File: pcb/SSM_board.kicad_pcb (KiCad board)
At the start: 4 copper layers, 100 x 100 mm, 115 parts, among them IC1 STPIC6C595TTR, IC2 STPIC6C595TTR, IC3 STPIC6C595TTR, IC4 STPIC6C595TTR, IC5 STPIC6C595TTR, J1 Conn_02x05_Top_Bottom, J2 Conn_02x05_Top_Bottom, U101 GAQY212GS, U102 GAQY212GS, U103 GAQY212GS, U104 GAQY212GS, U105 GAQY212GS, U106 GAQY212GS, U107 GAQY212GS, U108 GAQY212GS, U201 GAQY212GS, U202 GAQY212GS, U203 GAQY212GS, U204 GAQY212GS, U205 GAQY212GS, U206 GAQY212GS, U207 GAQY212GS, U208 GAQY212GS, U301 GAQY212GS, U302 GAQY212GS, U303 GAQY212GS, U304 GAQY212GS, U305 GAQY212GS, U306 GAQY212GS, U307 GAQY212GS, U308 GAQY212GS, U401 GAQY212GS, U402 GAQY212GS, U403 GAQY212GS, U404 GAQY212GS, U405 GAQY212GS, U406 GAQY212GS, U407 GAQY212GS, U408 GAQY212GS, U501 GAQY212GS, U502 GAQY212GS, U503 GAQY212GS, U504 GAQY212GS, U505 GAQY212GS, U506 GAQY212GS, U507 GAQY212GS, U508 GAQY212GS

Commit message: Functional block routing
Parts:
- removed J1, J2: Conn_02x05_Top_Bottom, Connector_IDC:IDC-Header_2x05_P2.54mm_Vertical
- added C6: 100n, Capacitor_SMD:C_0603_1608Metric_Pad1.08x0.95mm_HandSolder, F.Cu at (192.4, 129.0)
- added C7: 100n, Capacitor_SMD:C_0603_1608Metric_Pad1.08x0.95mm_HandSolder, F.Cu at (194.0, 137.6)
- added C8: 100n, Capacitor_SMD:C_0603_1608Metric_Pad1.08x0.95mm_HandSolder, F.Cu at (210.7, 129.0)
- added FB6: 100R @ 100MHz, Inductor_SMD:L_0603_1608Metric, F.Cu at (192.5, 125.6)
- added FB7: 100R @ 100MHz, Inductor_SMD:L_0603_1608Metric, F.Cu at (197.8, 141.5)
- added FB8: 100R @ 100MHz, Inductor_SMD:L_0603_1608Metric, F.Cu at (210.7, 125.8)
- added IC6: STPIC6C595TTR, SamacSys_Parts:SOP65P640X120-16N, F.Cu at (188.7, 131.1)
- added IC7: STPIC6C595TTR, SamacSys_Parts:SOP65P640X120-16N, F.Cu at (198.5, 130.9)
- added IC8: STPIC6C595TTR, SamacSys_Parts:SOP65P640X120-16N, F.Cu at (207.0, 131.1)
- added J701: DA15_Pins_MountingHoles, Connector_Dsub:DSUB-15_Pins_Horizontal_P2.77x2.84mm_EdgePinOffset4.94mm_Housed_MountingHolesOffset4.94mm, F.Cu at (77.8, 70.1)
- added J702: DA15_Pins_MountingHoles, Connector_Dsub:DSUB-15_Pins_Horizontal_P2.77x2.84mm_EdgePinOffset4.94mm_Housed_MountingHolesOffset4.94mm, F.Cu at (77.8, 110.5)
- added R6: 10k, Resistor_SMD:R_0603_1608Metric_Pad0.98x0.95mm_HandSolder, F.Cu at (191.0, 125.4)
- added R601: 50k, Resistor_SMD:R_0603_1608Metric_Pad0.98x0.95mm_HandSolder, F.Cu at (189.9, 96.1)
- added R602: 50k, Resistor_SMD:R_0603_1608Metric_Pad0.98x0.95mm_HandSolder, F.Cu at (189.9, 91.4)
- added R603: 50k, Resistor_SMD:R_0603_1608Metric_Pad0.98x0.95mm_HandSolder, F.Cu at (189.9, 86.8)
- added R604: 50k, Resistor_SMD:R_0603_1608Metric_Pad0.98x0.95mm_HandSolder, F.Cu at (189.9, 82.1)
- added R605: 50k, Resistor_SMD:R_0603_1608Metric_Pad0.98x0.95mm_HandSolder, F.Cu at (189.9, 63.5)
- added R606: 50k, Resistor_SMD:R_0603_1608Metric_Pad0.98x0.95mm_HandSolder, F.Cu at (189.9, 68.2)
- added R607: 50k, Resistor_SMD:R_0603_1608Metric_Pad0.98x0.95mm_HandSolder, F.Cu at (189.9, 72.8)
- added R608: 50k, Resistor_SMD:R_0603_1608Metric_Pad0.98x0.95mm_HandSolder, F.Cu at (189.9, 77.5)
- added R609: 50k, Resistor_SMD:R_0603_1608Metric_Pad0.98x0.95mm_HandSolder, F.Cu at (189.9, 114.7)
- added R610: 50k, Resistor_SMD:R_0603_1608Metric_Pad0.98x0.95mm_HandSolder, F.Cu at (189.9, 110.0)
- added R611: 50k, Resistor_SMD:R_0603_1608Metric_Pad0.98x0.95mm_HandSolder, F.Cu at (189.9, 105.4)
- added R612: 50k, Resistor_SMD:R_0603_1608Metric_Pad0.98x0.95mm_HandSolder, F.Cu at (189.9, 100.7)
- added R7: 10k, Resistor_SMD:R_0603_1608Metric_Pad0.98x0.95mm_HandSolder, F.Cu at (197.0, 137.8)
- added R701: 50k, Resistor_SMD:R_0603_1608Metric_Pad0.98x0.95mm_HandSolder, F.Cu at (205.6, 63.8)
- added R702: 50k, Resistor_SMD:R_0603_1608Metric_Pad0.98x0.95mm_HandSolder, F.Cu at (205.6, 68.5)
- added R703: 50k, Resistor_SMD:R_0603_1608Metric_Pad0.98x0.95mm_HandSolder, F.Cu at (205.6, 73.1)
- added R704: 50k, Resistor_SMD:R_0603_1608Metric_Pad0.98x0.95mm_HandSolder, F.Cu at (205.6, 77.8)
- added R705: 50k, Resistor_SMD:R_0603_1608Metric_Pad0.98x0.95mm_HandSolder, F.Cu at (205.6, 115.0)
- added R706: 50k, Resistor_SMD:R_0603_1608Metric_Pad0.98x0.95mm_HandSolder, F.Cu at (205.6, 110.3)
- added R707: 50k, Resistor_SMD:R_0603_1608Metric_Pad0.98x0.95mm_HandSolder, F.Cu at (205.6, 105.7)
- added R708: 50k, Resistor_SMD:R_0603_1608Metric_Pad0.98x0.95mm_HandSolder, F.Cu at (205.6, 101.0)
- added R709: 50k, Resistor_SMD:R_0603_1608Metric_Pad0.98x0.95mm_HandSolder, F.Cu at (205.6, 82.4)
- added R710: 50k, Resistor_SMD:R_0603_1608Metric_Pad0.98x0.95mm_HandSolder, F.Cu at (205.6, 87.1)
- added R711: 50k, Resistor_SMD:R_0603_1608Metric_Pad0.98x0.95mm_HandSolder, F.Cu at (205.6, 91.7)
- added R712: 50k, Resistor_SMD:R_0603_1608Metric_Pad0.98x0.95mm_HandSolder, F.Cu at (205.6, 96.4)
- added R8: 10k, Resistor_SMD:R_0603_1608Metric_Pad0.98x0.95mm_HandSolder, F.Cu at (209.1, 125.5)
- added RN11: 470R, Resistor_SMD:R_Array_Convex_4x0603, F.Cu at (188.3, 125.0)
- added RN12: 470R, Resistor_SMD:R_Array_Convex_4x0603, F.Cu at (185.3, 121.9)
- added RN13: 470R, Resistor_SMD:R_Array_Convex_4x0603, F.Cu at (195.1, 125.1)
- added RN14: 470R, Resistor_SMD:R_Array_Convex_4x0603, F.Cu at (198.9, 125.1)
- added RN15: 470R, Resistor_SMD:R_Array_Convex_4x0603, F.Cu at (206.5, 125.1)
- added RN16: 470R, Resistor_SMD:R_Array_Convex_4x0603, F.Cu at (202.8, 125.1)
- added U601: GAQY212GS, Package_SO:SOP-4_3.8x4.1mm_P2.54mm, F.Cu at (194.4, 96.1)
- added U602: GAQY212GS, Package_SO:SOP-4_3.8x4.1mm_P2.54mm, F.Cu at (194.4, 91.4)
- added U603: GAQY212GS, Package_SO:SOP-4_3.8x4.1mm_P2.54mm, F.Cu at (194.4, 86.8)
- added U604: GAQY212GS, Package_SO:SOP-4_3.8x4.1mm_P2.54mm, F.Cu at (194.4, 82.1)
- added U605: GAQY212GS, Package_SO:SOP-4_3.8x4.1mm_P2.54mm, F.Cu at (194.4, 63.5)
- added U606: GAQY212GS, Package_SO:SOP-4_3.8x4.1mm_P2.54mm, F.Cu at (194.4, 68.2)
- added U607: GAQY212GS, Package_SO:SOP-4_3.8x4.1mm_P2.54mm, F.Cu at (194.4, 72.8)
- added U608: GAQY212GS, Package_SO:SOP-4_3.8x4.1mm_P2.54mm, F.Cu at (194.4, 77.5)
- added U609: GAQY212GS, Package_SO:SOP-4_3.8x4.1mm_P2.54mm, F.Cu at (194.4, 114.7)
- added U610: GAQY212GS, Package_SO:SOP-4_3.8x4.1mm_P2.54mm, F.Cu at (194.4, 110.0)
- added U611: GAQY212GS, Package_SO:SOP-4_3.8x4.1mm_P2.54mm, F.Cu at (194.4, 105.4)
- added U612: GAQY212GS, Package_SO:SOP-4_3.8x4.1mm_P2.54mm, F.Cu at (194.4, 100.7)
- added U701: GAQY212GS, Package_SO:SOP-4_3.8x4.1mm_P2.54mm, F.Cu at (210.1, 63.8)
- added U702: GAQY212GS, Package_SO:SOP-4_3.8x4.1mm_P2.54mm, F.Cu at (210.1, 68.5)
- added U703: GAQY212GS, Package_SO:SOP-4_3.8x4.1mm_P2.54mm, F.Cu at (210.1, 73.1)
- added U704: GAQY212GS, Package_SO:SOP-4_3.8x4.1mm_P2.54mm, F.Cu at (210.1, 77.8)
- added U705: GAQY212GS, Package_SO:SOP-4_3.8x4.1mm_P2.54mm, F.Cu at (210.1, 115.0)
- added U706: GAQY212GS, Package_SO:SOP-4_3.8x4.1mm_P2.54mm, F.Cu at (210.1, 110.3)
- added U707: GAQY212GS, Package_SO:SOP-4_3.8x4.1mm_P2.54mm, F.Cu at (210.1, 105.7)
- added U708: GAQY212GS, Package_SO:SOP-4_3.8x4.1mm_P2.54mm, F.Cu at (210.1, 101.0)
- added U709: GAQY212GS, Package_SO:SOP-4_3.8x4.1mm_P2.54mm, F.Cu at (210.1, 82.4)
- added U710: GAQY212GS, Package_SO:SOP-4_3.8x4.1mm_P2.54mm, F.Cu at (210.1, 87.1)
- added U711: GAQY212GS, Package_SO:SOP-4_3.8x4.1mm_P2.54mm, F.Cu at (210.1, 91.7)
- added U712: GAQY212GS, Package_SO:SOP-4_3.8x4.1mm_P2.54mm, F.Cu at (210.1, 96.4)
- moved R505 140.9 mm to (118.0, 67.6)
- moved FB5 137.8 mm to (156.3, 64.6), turned to 180 degrees
- moved R506 136.8 mm to (122.6, 67.6)
- moved R5 134.9 mm to (156.1, 66.1)
- moved R405 134.6 mm to (118.0, 83.4)
- moved R507 132.8 mm to (127.3, 67.6)
- moved C5 131.2 mm to (159.7, 65.0), turned to 180 degrees
- moved R406 130.1 mm to (122.6, 83.4)
- moved R305 130.1 mm to (118.0, 99.1)
- moved R508 128.9 mm to (131.9, 67.6)
- moved IC5 127.0 mm to (161.7, 68.7)
- moved R407 125.8 mm to (127.3, 83.4)
- moved R306 125.3 mm to (122.6, 99.1)
- moved R504 122.1 mm to (136.6, 67.6)
- moved R408 121.5 mm to (131.9, 83.4)
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- renumbered R102 to R101, R103 to R102, R104 to R103, R105 to R104, R106 to R105, R107 to R106, R108 to R107, R109 to R108
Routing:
- net +5V: track 134.1 -> 385.1 mm
- net /Frontend/701: track 0.00 -> 62.7 mm
- net /Frontend/605: track 0.00 -> 58.9 mm
- net /Frontend/702: track 0.00 -> 57.7 mm
- net /Frontend/606: track 0.00 -> 54.1 mm
- net /Frontend/703: track 0.00 -> 52.7 mm
- net /Frontend/607: track 0.00 -> 49.4 mm
- net /Frontend/704: track 0.00 -> 47.7 mm
- net /Frontend/608: track 0.00 -> 44.6 mm
- net /Frontend/604: track 0.00 -> 43.0 mm
- net /Frontend/709: track 0.00 -> 42.5 mm
- net /Frontend/505: track 0.00 -> 40.9 mm
- net /Frontend/305: track 0.00 -> 40.8 mm
- net /Frontend/405: track 0.00 -> 40.8 mm
- net /Frontend/603: track 0.00 -> 38.3 mm
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
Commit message: More routing
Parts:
- moved R7 106.7 mm to (90.3, 140.5), turned to 90 degrees
- moved FB7 105.3 mm to (93.4, 127.1), turned to 90 degrees
- moved IC7 102.7 mm to (96.1, 138.9)
- moved IC6 102.7 mm to (86.3, 138.2)
- moved R701 102.7 mm to (103.2, 71.0)
- moved R702 102.7 mm to (103.2, 75.7)
- moved R703 102.7 mm to (103.2, 80.3)
- moved R704 102.7 mm to (103.2, 85.0)
- moved R705 102.7 mm to (103.2, 122.2)
- moved R706 102.7 mm to (103.2, 117.5)
- moved R707 102.7 mm to (103.2, 112.9)
- moved R708 102.7 mm to (103.2, 108.2)
- moved R709 102.7 mm to (103.2, 89.6)
- moved R710 102.7 mm to (103.2, 94.3)
- moved R711 102.7 mm to (103.2, 98.9)
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- renumbered J701 to J1, J702 to J2
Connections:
- J1 pad 1: Net-(J701-Pad1) -> Net-(J1-Pad1)
- J1 pad 10: Net-(J701-P10) -> Net-(J1-P10)
- J1 pad 11: Net-(J701-P111) -> Net-(J1-P111)
- J1 pad 12: Net-(J701-P12) -> Net-(J1-P12)
- J1 pad 13: Net-(J701-P13) -> Net-(J1-P13)
- J1 pad 14: Net-(J701-P14) -> Earth_Protective
- J1 pad 2: Net-(J701-Pad2) -> Net-(J1-Pad2)
- J1 pad 3: Net-(J701-Pad3) -> Net-(J1-Pad3)
- J1 pad 4: Net-(J701-Pad4) -> Net-(J1-Pad4)
- J1 pad 5: Net-(J701-Pad5) -> Net-(J1-Pad5)
- J1 pad 6: Net-(J701-Pad6) -> Net-(J1-Pad6)
- J1 pad 7: Net-(J701-Pad7) -> Net-(J1-Pad7)
- J1 pad 8: Net-(J701-Pad8) -> Net-(J1-Pad8)
- J1 pad 9: Net-(J701-P9) -> Net-(J1-P9)
- J2 pad 1: Net-(J702-Pad1) -> Net-(J2-Pad1)
- J2 pad 10: Net-(J702-P10) -> Net-(J2-P10)
- J2 pad 11: Net-(J702-P111) -> Net-(J2-P111)
- J2 pad 12: Net-(J702-P12) -> Net-(J2-P12)
- J2 pad 13: Net-(J702-P13) -> Net-(J2-P13)
- J2 pad 14: unconnected-(J702-P14-Pad14) -> Net-(J2-P14)
- J2 pad 15: unconnected-(J702-P15-Pad15) -> Earth_Protective
- J2 pad 2: Net-(J702-Pad2) -> Net-(J2-Pad2)
- J2 pad 3: Net-(J702-Pad3) -> Net-(J2-Pad3)
- J2 pad 4: Net-(J702-Pad4) -> Net-(J2-Pad4)
- J2 pad 5: Net-(J702-Pad5) -> Net-(J2-Pad5)
- J2 pad 6: Net-(J702-Pad6) -> Net-(J2-Pad6)
- J2 pad 7: Net-(J702-Pad7) -> Net-(J2-Pad7)
- J2 pad 8: Net-(J702-Pad8) -> Net-(J2-Pad8)
- J2 pad 9: Net-(J702-P9) -> Net-(J2-P9)
- U101 pad 3: Net-(J702-Pad6) -> Net-(J1-Pad6)
- U101 pad 4: Net-(J702-Pad1) -> Net-(J1-Pad1)
- U102 pad 3: Net-(J702-Pad7) -> Net-(J1-Pad7)
- U102 pad 4: Net-(J702-Pad1) -> Net-(J1-Pad1)
- U103 pad 3: Net-(J702-Pad8) -> Net-(J1-Pad8)
- U103 pad 4: Net-(J702-Pad1) -> Net-(J1-Pad1)
- U104 pad 3: Net-(J702-P9) -> Net-(J1-P9)
- U104 pad 4: Net-(J702-Pad1) -> Net-(J1-Pad1)
- U105 pad 3: Net-(J702-P10) -> Net-(J1-P10)
- U105 pad 4: Net-(J702-Pad1) -> Net-(J1-Pad1)
- U106 pad 3: Net-(J702-P111) -> Net-(J1-P111)
- U106 pad 4: Net-(J702-Pad1) -> Net-(J1-Pad1)
- U107 pad 3: Net-(J702-P12) -> Net-(J1-P12)
- U107 pad 4: Net-(J702-Pad1) -> Net-(J1-Pad1)
- U108 pad 3: Net-(J702-P13) -> Net-(J1-P13)
- U108 pad 4: Net-(J702-Pad1) -> Net-(J1-Pad1)
- U201 pad 3: Net-(J702-Pad6) -> Net-(J1-Pad6)
- U201 pad 4: Net-(J702-Pad2) -> Net-(J1-Pad2)
- U202 pad 3: Net-(J702-Pad7) -> Net-(J1-Pad7)
- U202 pad 4: Net-(J702-Pad2) -> Net-(J1-Pad2)
- U203 pad 3: Net-(J702-Pad8) -> Net-(J1-Pad8)
- U203 pad 4: Net-(J702-Pad2) -> Net-(J1-Pad2)
- U204 pad 3: Net-(J702-P9) -> Net-(J1-P9)
- U204 pad 4: Net-(J702-Pad2) -> Net-(J1-Pad2)
- U205 pad 3: Net-(J702-P10) -> Net-(J1-P10)
- U205 pad 4: Net-(J702-Pad2) -> Net-(J1-Pad2)
- U206 pad 3: Net-(J702-P111) -> Net-(J1-P111)
- U206 pad 4: Net-(J702-Pad2) -> Net-(J1-Pad2)
- U207 pad 3: Net-(J702-P12) -> Net-(J1-P12)
- U207 pad 4: Net-(J702-Pad2) -> Net-(J1-Pad2)
- U208 pad 3: Net-(J702-P13) -> Net-(J1-P13)
- U208 pad 4: Net-(J702-Pad2) -> Net-(J1-Pad2)
- U301 pad 3: Net-(J702-Pad6) -> Net-(J1-Pad6)
- U301 pad 4: Net-(J702-Pad3) -> Net-(J1-Pad3)
- U302 pad 3: Net-(J702-Pad7) -> Net-(J1-Pad7)
- U302 pad 4: Net-(J702-Pad3) -> Net-(J1-Pad3)
- U303 pad 3: Net-(J702-Pad8) -> Net-(J1-Pad8)
- U303 pad 4: Net-(J702-Pad3) -> Net-(J1-Pad3)
- U304 pad 3: Net-(J702-P9) -> Net-(J1-P9)
- U304 pad 4: Net-(J702-Pad3) -> Net-(J1-Pad3)
- U305 pad 3: Net-(J702-P10) -> Net-(J1-P10)
- U305 pad 4: Net-(J702-Pad3) -> Net-(J1-Pad3)
- U306 pad 3: Net-(J702-P111) -> Net-(J1-P111)
- U306 pad 4: Net-(J702-Pad3) -> Net-(J1-Pad3)
- U307 pad 3: Net-(J702-P12) -> Net-(J1-P12)
- U307 pad 4: Net-(J702-Pad3) -> Net-(J1-Pad3)
- U308 pad 3: Net-(J702-P13) -> Net-(J1-P13)
- U308 pad 4: Net-(J702-Pad3) -> Net-(J1-Pad3)
- U401 pad 3: Net-(J702-Pad6) -> Net-(J1-Pad6)
- U401 pad 4: Net-(J702-Pad4) -> Net-(J1-Pad4)
- U402 pad 3: Net-(J702-Pad7) -> Net-(J1-Pad7)
- U402 pad 4: Net-(J702-Pad4) -> Net-(J1-Pad4)
- U403 pad 3: Net-(J702-Pad8) -> Net-(J1-Pad8)
- U403 pad 4: Net-(J702-Pad4) -> Net-(J1-Pad4)
- U404 pad 3: Net-(J702-P9) -> Net-(J1-P9)
- U404 pad 4: Net-(J702-Pad4) -> Net-(J1-Pad4)
- U405 pad 3: Net-(J702-P10) -> Net-(J1-P10)
- U405 pad 4: Net-(J702-Pad4) -> Net-(J1-Pad4)
- U406 pad 3: Net-(J702-P111) -> Net-(J1-P111)
- U406 pad 4: Net-(J702-Pad4) -> Net-(J1-Pad4)
- U407 pad 3: Net-(J702-P12) -> Net-(J1-P12)
- U407 pad 4: Net-(J702-Pad4) -> Net-(J1-Pad4)
- U408 pad 3: Net-(J702-P13) -> Net-(J1-P13)
- U408 pad 4: Net-(J702-Pad4) -> Net-(J1-Pad4)
- U501 pad 3: Net-(J702-Pad6) -> Net-(J1-Pad6)
- U501 pad 4: Net-(J702-Pad5) -> Net-(J1-Pad5)
- U502 pad 3: Net-(J702-Pad7) -> Net-(J1-Pad7)
- U502 pad 4: Net-(J702-Pad5) -> Net-(J1-Pad5)
- U503 pad 3: Net-(J702-Pad8) -> Net-(J1-Pad8)
- U503 pad 4: Net-(J702-Pad5) -> Net-(J1-Pad5)
- U504 pad 3: Net-(J702-P9) -> Net-(J1-P9)
- U504 pad 4: Net-(J702-Pad5) -> Net-(J1-Pad5)
- U505 pad 3: Net-(J702-P10) -> Net-(J1-P10)
- U505 pad 4: Net-(J702-Pad5) -> Net-(J1-Pad5)
- U506 pad 3: Net-(J702-P111) -> Net-(J1-P111)
- U506 pad 4: Net-(J702-Pad5) -> Net-(J1-Pad5)
- U507 pad 3: Net-(J702-P12) -> Net-(J1-P12)
- U507 pad 4: Net-(J702-Pad5) -> Net-(J1-Pad5)
- U508 pad 3: Net-(J702-P13) -> Net-(J1-P13)
- U508 pad 4: Net-(J702-Pad5) -> Net-(J1-Pad5)
- U601 pad 3: Net-(J701-Pad3) -> Net-(J2-Pad3)
- U601 pad 4: Net-(J701-Pad1) -> Net-(J2-Pad1)
- U602 pad 3: Net-(J701-Pad4) -> Net-(J2-Pad4)
- U602 pad 4: Net-(J701-Pad1) -> Net-(J2-Pad1)
- U603 pad 3: Net-(J701-Pad5) -> Net-(J2-Pad5)
- U603 pad 4: Net-(J701-Pad1) -> Net-(J2-Pad1)
- U604 pad 3: Net-(J701-Pad6) -> Net-(J2-Pad6)
- U604 pad 4: Net-(J701-Pad1) -> Net-(J2-Pad1)
- U605 pad 3: Net-(J701-Pad7) -> Net-(J2-Pad7)
- U605 pad 4: Net-(J701-Pad1) -> Net-(J2-Pad1)
- U606 pad 3: Net-(J701-Pad8) -> Net-(J2-Pad8)
- U606 pad 4: Net-(J701-Pad1) -> Net-(J2-Pad1)
- U607 pad 3: Net-(J701-P9) -> Net-(J2-P9)
- U607 pad 4: Net-(J701-Pad1) -> Net-(J2-Pad1)
- U608 pad 3: Net-(J701-P10) -> Net-(J2-P10)
- U608 pad 4: Net-(J701-Pad1) -> Net-(J2-Pad1)
- U609 pad 3: Net-(J701-P111) -> Net-(J2-P111)
- U609 pad 4: unconnected-(U609-Pad4) -> Net-(J2-Pad1)
- U610 pad 3: Net-(J701-P12) -> Net-(J2-P12)
- U610 pad 4: Net-(J701-Pad1) -> Net-(J2-Pad1)
- U611 pad 3: Net-(J701-P13) -> Net-(J2-P13)
- U611 pad 4: Net-(J701-Pad1) -> Net-(J2-Pad1)
- U612 pad 3: Net-(J701-P14) -> Net-(J2-P14)
- U612 pad 4: Net-(J701-Pad1) -> Net-(J2-Pad1)
- U701 pad 3: Net-(J701-Pad3) -> Net-(J2-Pad3)
- U701 pad 4: Net-(J701-Pad2) -> Net-(J2-Pad2)
- U702 pad 3: Net-(J701-Pad4) -> Net-(J2-Pad4)
- U702 pad 4: Net-(J701-Pad2) -> Net-(J2-Pad2)
- U703 pad 3: Net-(J701-Pad5) -> Net-(J2-Pad5)
- U703 pad 4: Net-(J701-Pad2) -> Net-(J2-Pad2)
- U704 pad 3: Net-(J701-Pad6) -> Net-(J2-Pad6)
- U704 pad 4: Net-(J701-Pad2) -> Net-(J2-Pad2)
- U705 pad 3: Net-(J701-Pad7) -> Net-(J2-Pad7)
- U705 pad 4: Net-(J701-Pad2) -> Net-(J2-Pad2)
- U706 pad 3: Net-(J701-Pad8) -> Net-(J2-Pad8)
- U706 pad 4: Net-(J701-Pad2) -> Net-(J2-Pad2)
- U707 pad 3: Net-(J701-P9) -> Net-(J2-P9)
- U707 pad 4: Net-(J701-Pad2) -> Net-(J2-Pad2)
- U708 pad 3: Net-(J701-P10) -> Net-(J2-P10)
- U708 pad 4: Net-(J701-Pad2) -> Net-(J2-Pad2)
- U709 pad 3: Net-(J701-P111) -> Net-(J2-P111)
- U709 pad 4: unconnected-(U709-Pad4) -> Net-(J2-Pad2)
- U710 pad 3: Net-(J701-P12) -> Net-(J2-P12)
- U710 pad 4: Net-(J701-Pad2) -> Net-(J2-Pad2)
- U711 pad 3: Net-(J701-P13) -> Net-(J2-P13)
- U711 pad 4: Net-(J701-Pad2) -> Net-(J2-Pad2)
- U712 pad 3: Net-(J701-P14) -> Net-(J2-P14)
- U712 pad 4: Net-(J701-Pad2) -> Net-(J2-Pad2)
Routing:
- net +5V: track 385.1 -> 622.6 mm, vias 1 -> 3
- net Net-(J2-Pad2): track 0.00 -> 135.9 mm, vias 0 -> 3
- net Net-(J2-Pad1): track 0.00 -> 128.2 mm, vias 0 -> 3
- net Net-(J2-Pad3): track 0.00 -> 113.5 mm, vias 0 -> 4
- net Net-(J2-P10): track 0.00 -> 107.5 mm, vias 0 -> 4
- net Net-(J2-Pad4): track 0.00 -> 102.6 mm, vias 0 -> 4
- net Net-(J2-P111): track 0.00 -> 102.3 mm, vias 0 -> 4
- net Net-(J2-P9): track 0.00 -> 95.9 mm, vias 0 -> 4
- net Net-(J2-Pad8): track 0.00 -> 94.6 mm, vias 0 -> 4
- net Net-(J2-P12): track 0.00 -> 94.5 mm, vias 0 -> 4
- net Net-(J2-Pad7): track 0.00 -> 93.4 mm, vias 0 -> 4
- net Net-(J2-Pad5): track 0.00 -> 89.8 mm, vias 0 -> 4
- net Net-(J2-P13): track 0.00 -> 87.1 mm, vias 0 -> 4
- net Net-(J2-P14): track 0.00 -> 83.3 mm, vias 0 -> 4
- net Net-(J2-Pad6): track 0.00 -> 78.2 mm, vias 0 -> 4
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- added copper zone on B.Cu, net Earth_Protective
- added copper zone on In2.Cu, net Earth_Protective
- added copper zone on F.Cu, net Net-(J2-P10)
- added copper zone on F.Cu, net Net-(J2-P111)
- added copper zone on F.Cu, net Net-(J2-P12)
- added copper zone on F.Cu, net Net-(J2-P13)
- added copper zone on F.Cu, net Net-(J2-P14)
- added copper zone on F.Cu, net Net-(J2-P9)
- added copper zone on F.Cu, net Net-(J2-Pad3)
- added copper zone on F.Cu, net Net-(J2-Pad4)
- added copper zone on F.Cu, net Net-(J2-Pad5)
- added copper zone on F.Cu, net Net-(J2-Pad6)
- added copper zone on F.Cu, net Net-(J2-Pad7)
- added copper zone on F.Cu, net Net-(J2-Pad8)
- removed copper zone on B.Cu, net GND
- removed copper zone on In2.Cu, net GND

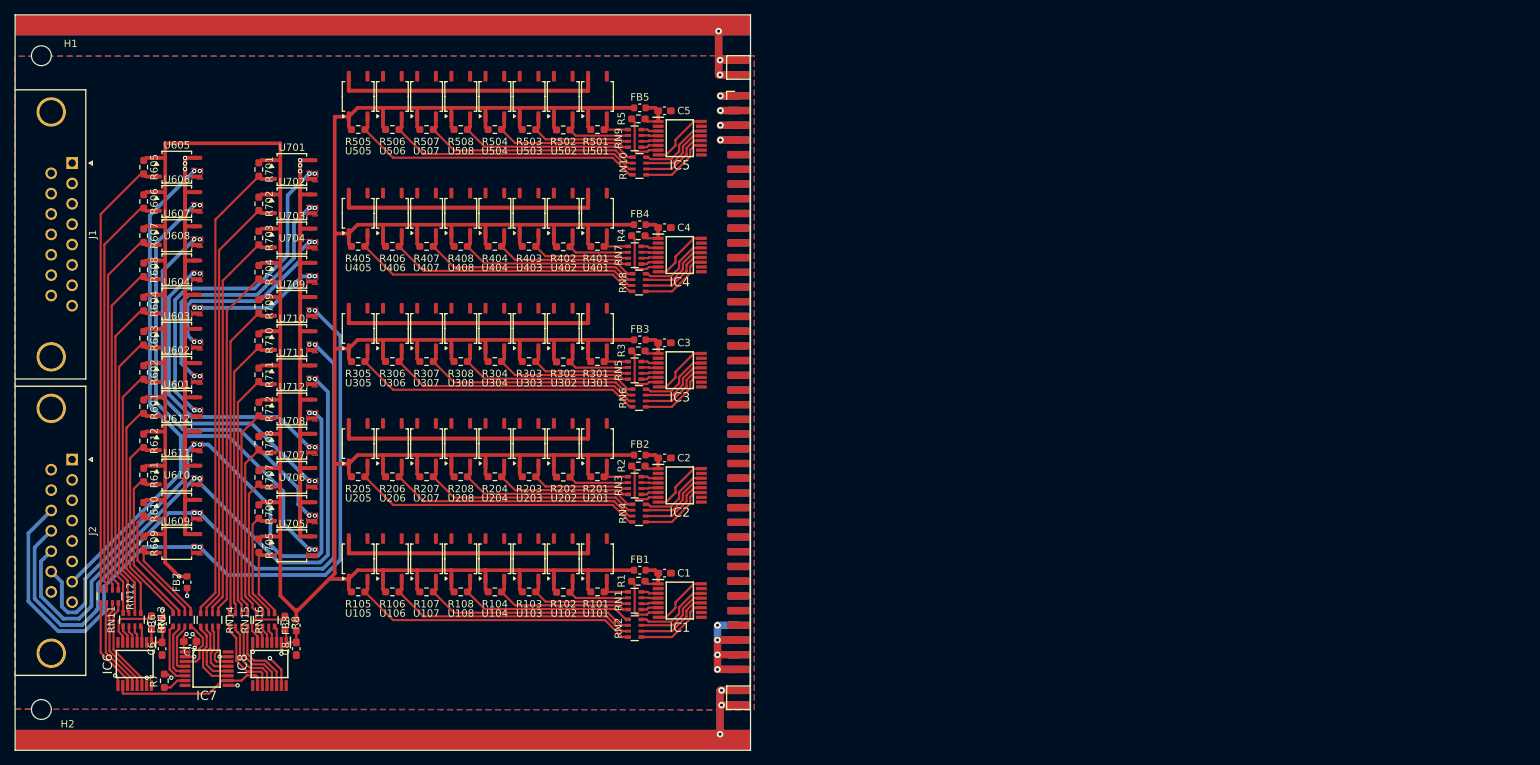
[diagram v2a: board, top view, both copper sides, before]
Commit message: Routing done, left via stitching and silkscreen collisions
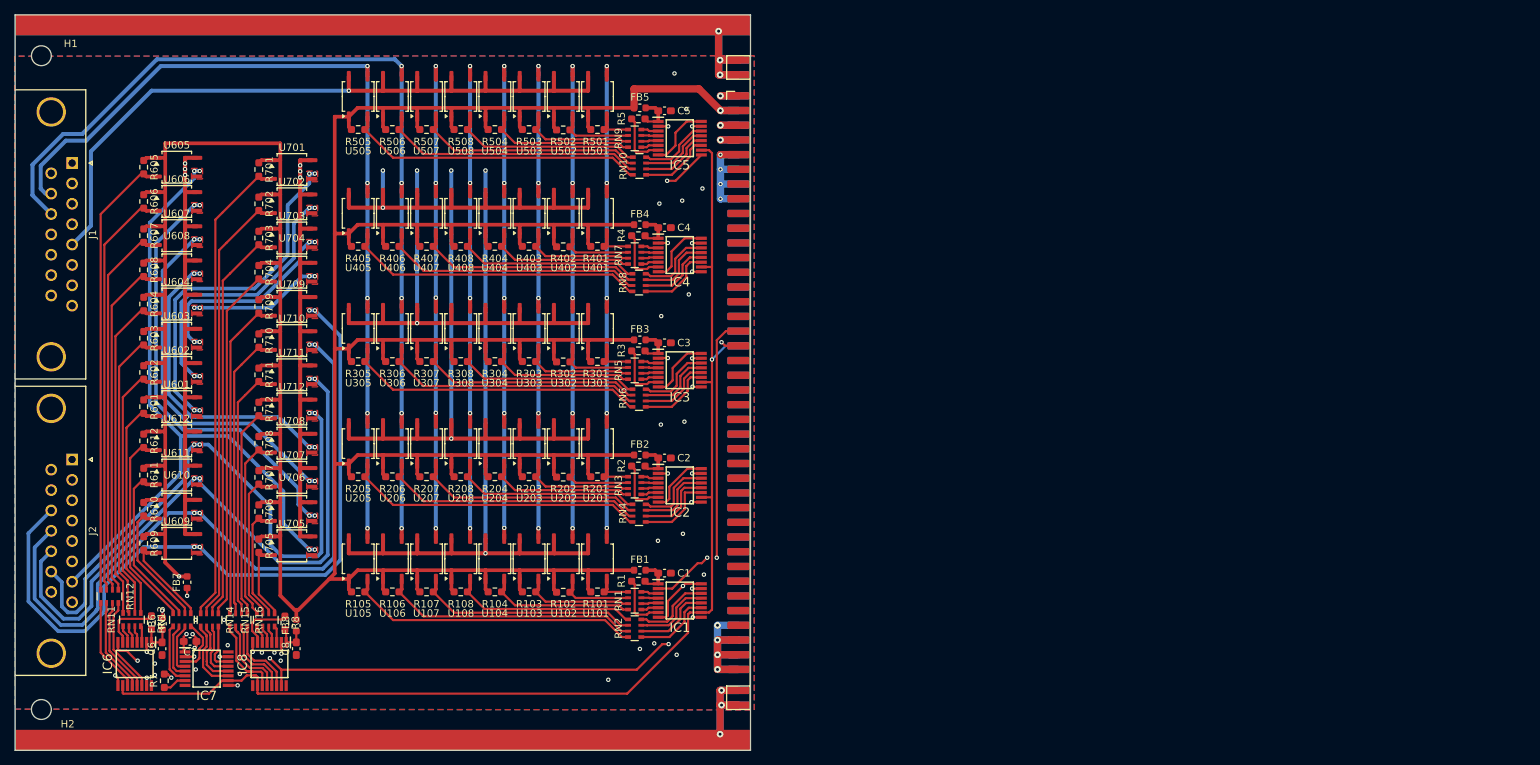
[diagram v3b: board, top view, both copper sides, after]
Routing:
- net Net-(J1-Pad6): track 0.00 -> 166.6 mm, vias 0 -> 5
- net Net-(J1-Pad7): track 0.00 -> 165.9 mm, vias 0 -> 5
- net Net-(J1-Pad8): track 0.00 -> 162.5 mm, vias 0 -> 5
- net /Frontend/Driver4/SER_OUT: track 0.00 -> 156.0 mm, vias 0 -> 2
- net Net-(J1-P13): track 0.00 -> 148.9 mm, vias 0 -> 5
- net /Conn/SSR_SCK: track 25.6 -> 168.7 mm, vias 3 -> 10
- net /Conn/SSR_CS: track 21.7 -> 163.1 mm, vias 0 -> 1
- net Net-(J1-P12): track 0.00 -> 139.3 mm, vias 0 -> 5
- net Net-(J1-P9): track 0.00 -> 138.3 mm, vias 0 -> 5
- net Net-(J1-P111): track 0.00 -> 134.1 mm, vias 0 -> 5
- net Net-(J1-Pad1): track 36.5 -> 164.1 mm, vias 0 -> 2
- net Net-(J1-P10): track 0.00 -> 124.6 mm, vias 0 -> 5
- net Net-(J1-Pad2): track 36.7 -> 147.6 mm, vias 0 -> 2
- net Net-(J1-Pad3): track 36.6 -> 128.5 mm, vias 0 -> 2
- net Net-(J1-Pad4): track 36.5 -> 106.5 mm, vias 0 -> 2
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
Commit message: Add earth symbols, capacitors and teardrops
Add protective earth/earth power symbols and instances to the Conn schematic, plus wiring/junctions to connect them. Add three SMD capacitors (C9, C10, C11) to the schematic and link them to a 1206 hand-solder capacitor footprint. Update PCB (SSM_board.kicad_pcb): add the 1206 hand-solder footprint, assign nets for Earth_Protective and GND, adjust two resistor silk text positions, and enable teardrops (with parameters) on many pads to improve manufacturability. Minor .kicad_pro update included.
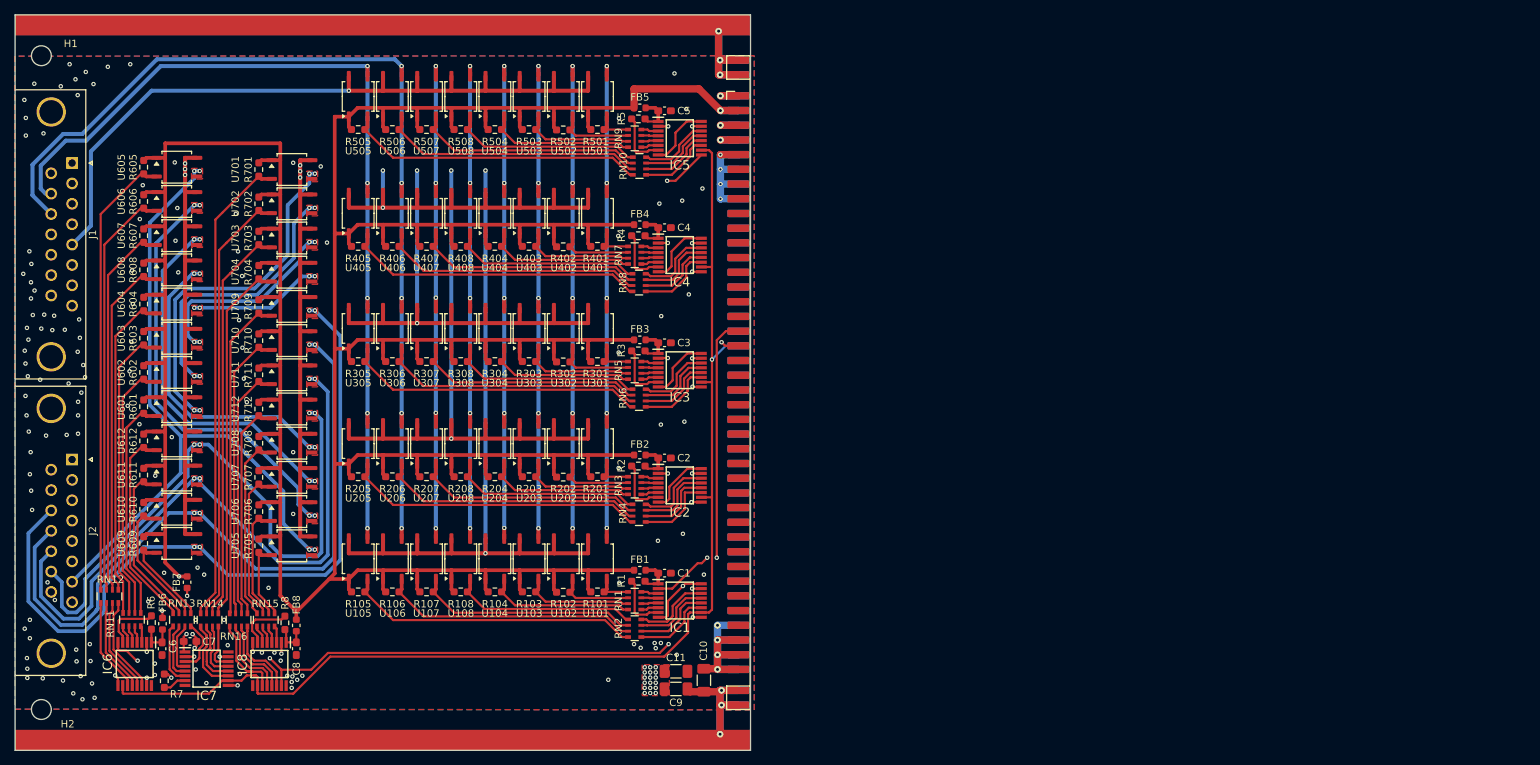
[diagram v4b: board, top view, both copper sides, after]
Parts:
- added C10: 1nF/2kV, Capacitor_SMD:C_1206_3216Metric_Pad1.33x1.80mm_HandSolder, F.Cu at (163.7, 140.5)
- added C11: 1nF/2kV, Capacitor_SMD:C_1206_3216Metric_Pad1.33x1.80mm_HandSolder, F.Cu at (159.9, 139.2)
- added C9: 1nF/2kV, Capacitor_SMD:C_1206_3216Metric_Pad1.33x1.80mm_HandSolder, F.Cu at (159.9, 141.7)
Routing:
- net Earth: track 147.7 -> 152.4 mm
- net GND: track 99.9 -> 101.8 mm, vias 40 -> 75
- net /Frontend/Driver6/SER_OUT: track 13.3 -> 12.3 mm
- net Earth_Protective: vias 0 -> 97
- added copper zone on F.Cu, net Earth_Protective
